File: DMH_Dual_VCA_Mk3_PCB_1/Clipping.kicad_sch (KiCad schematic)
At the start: 43 parts, among them SW1 SW_DPDT_OnOffOn_x2, U4 TL074, U8 TL074

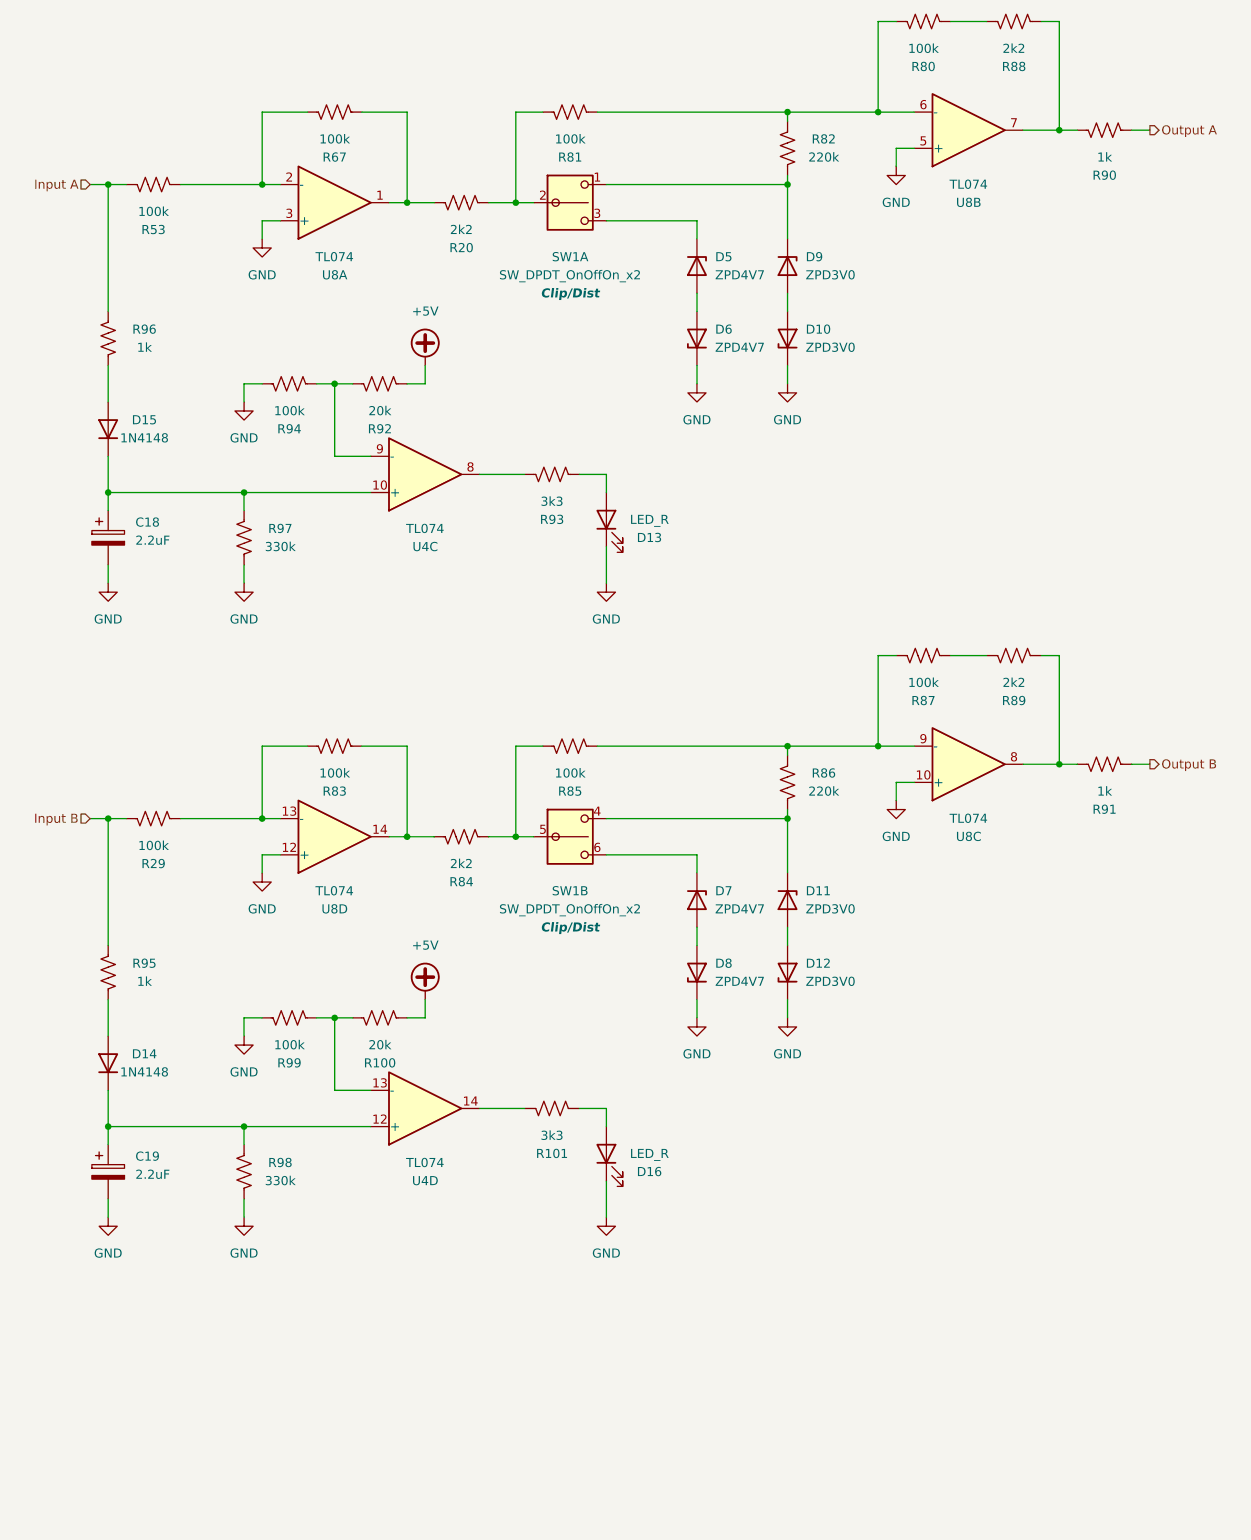
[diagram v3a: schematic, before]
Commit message: Improved cipping indication LED drive
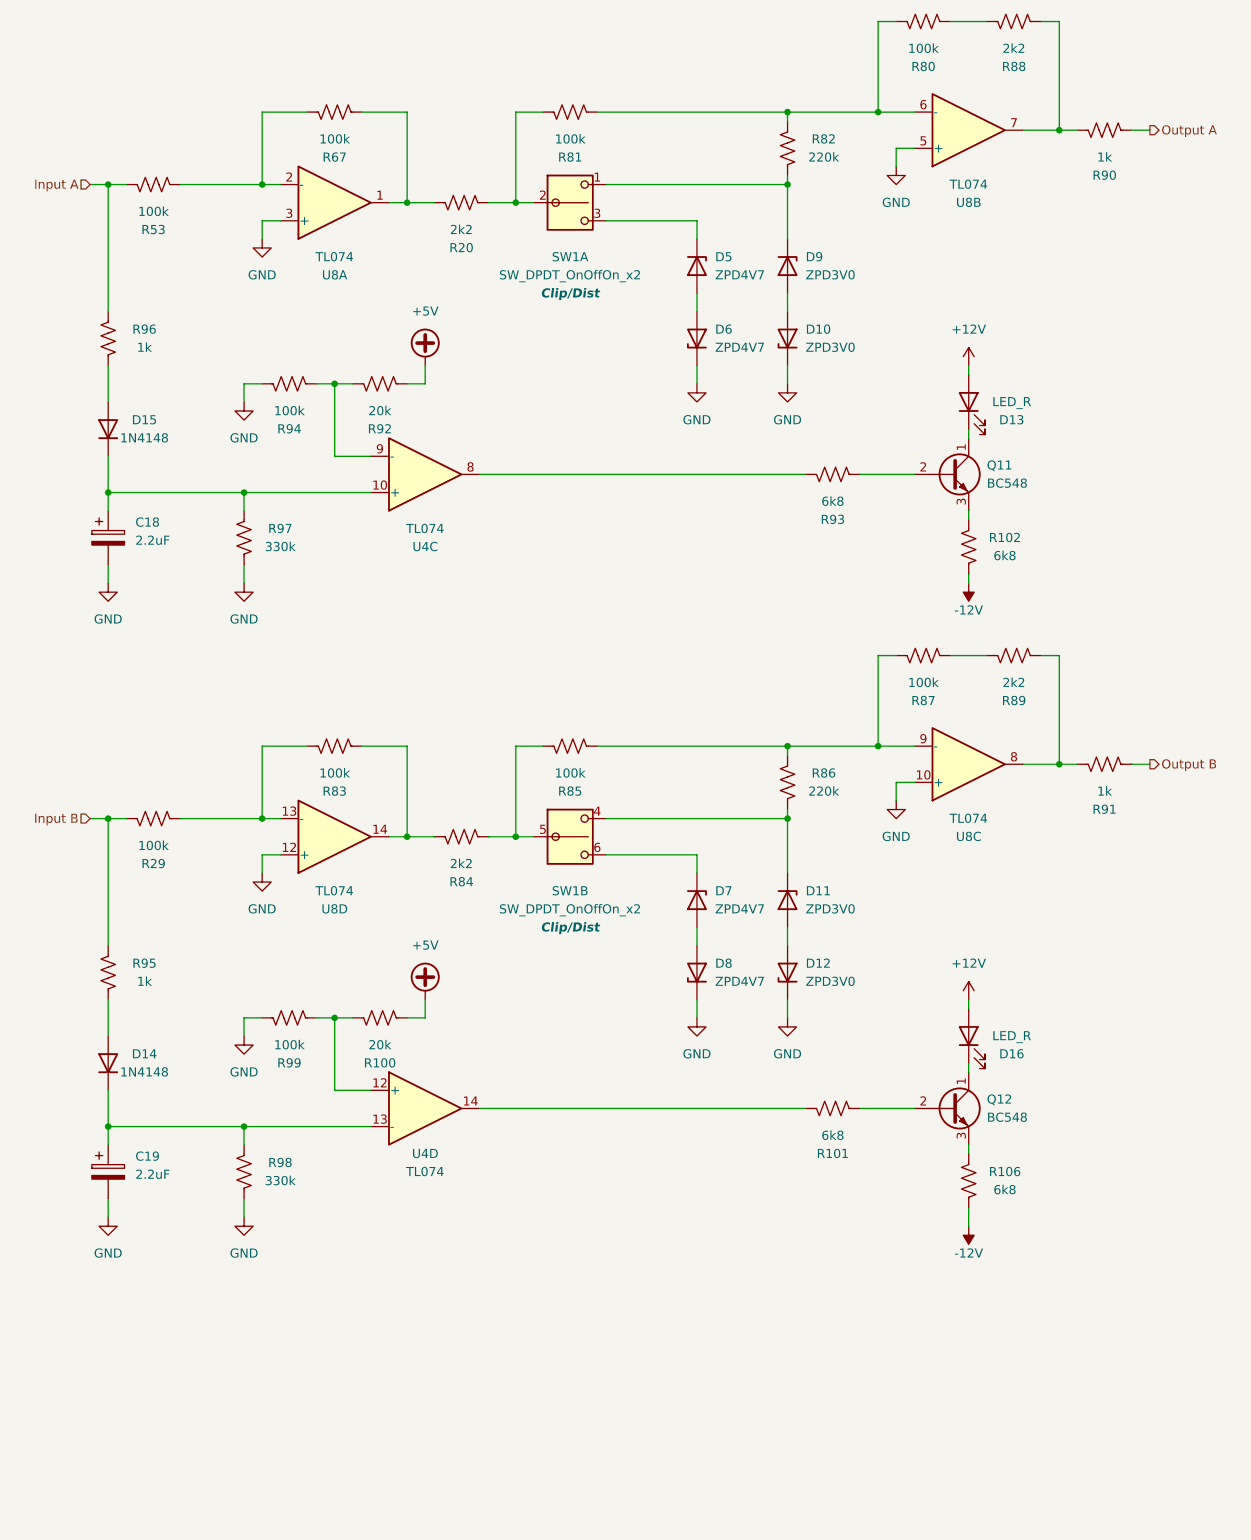
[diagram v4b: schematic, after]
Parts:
- added Q11: BC548, Package_TO_SOT_THT:TO-92_Inline, symbol Transistor_BJT:BC548
- added Q12: BC548, Package_TO_SOT_THT:TO-92L_Inline_Wide, symbol Transistor_BJT:BC548
- added R102, R106: 6k8, Resistor_THT:R_Axial_DIN0207_L6.3mm_D2.5mm_P7.62mm_Horizontal, symbol Device:R_US
- R101, R93: value 3k3 -> 6k8
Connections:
- net GND: no longer D13.1 (K), D16.1 (K)
- net at R93.2: now also Q11.2 (B); no longer D13.2 (A)
- net at R101.2: now also Q12.2 (B); no longer D16.2 (A)
- net at C19.1, D14.1 (K), R98.2: now also U4.13 (-); no longer U4.12 (+)
- net at R100.1, R99.2: now also U4.12 (+); no longer U4.13 (-)
- new net: D13.1 (K), Q11.1 (C)
- new net: Q11.3 (E), R102.2
- new net: D16.1 (K), Q12.1 (C)
- new net: Q12.3 (E), R106.2
- new net +12V: D13.2 (A), D16.2 (A)
- new net -12V: R102.1, R106.1
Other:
- moved on the sheet: D13, D16, R101, R93

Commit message: Improved clipping indicator
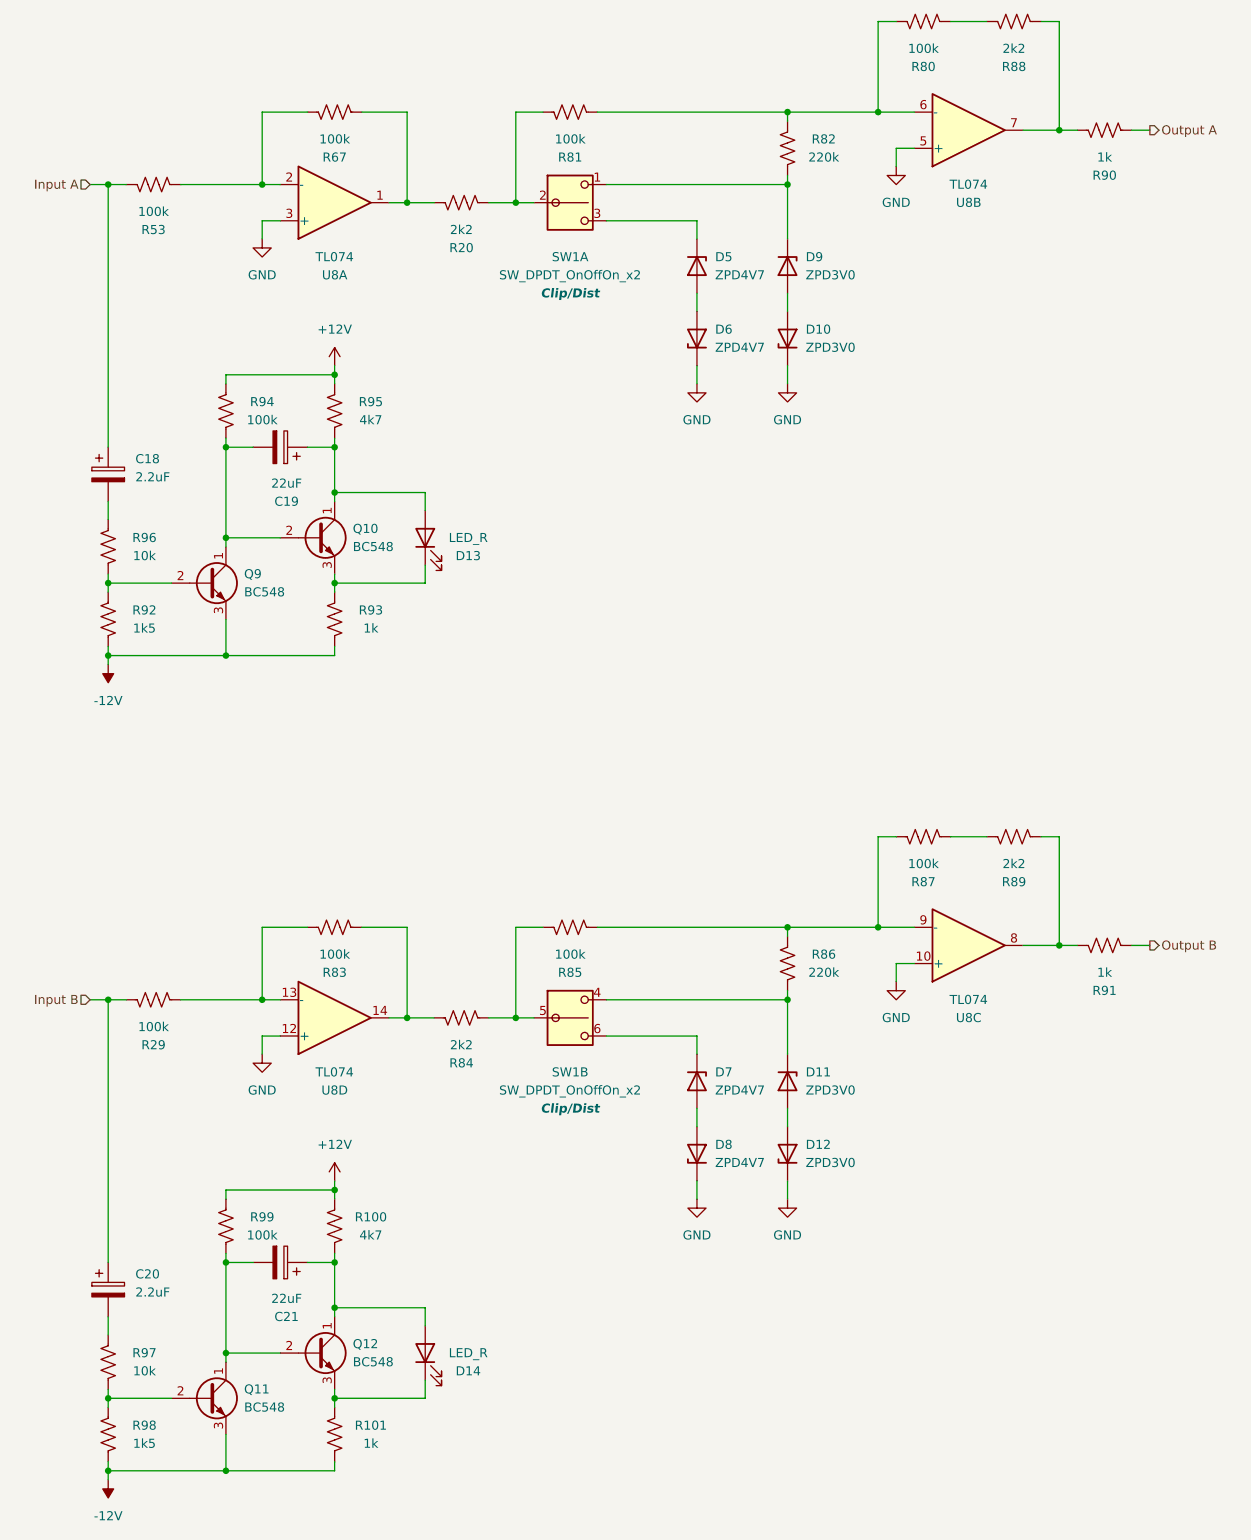
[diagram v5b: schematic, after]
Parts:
- removed D14, D15: 1N4148, Diode_THT:D_DO-35_SOD27_P7.62mm_Horizontal, symbol Diode:1N4148
- removed D16: LED_R, LED_THT:LED_D3.0mm, symbol Device:LED
- removed R102, R106: 6k8, Resistor_THT:R_Axial_DIN0207_L6.3mm_D2.5mm_P7.62mm_Horizontal, symbol Device:R_US
- removed U4: TL074, Package_DIP:DIP-14_W7.62mm_Socket, symbol Amplifier_Operational:TL074
- added C20: 2.2uF, Capacitor_THT:CP_Radial_D4.0mm_P1.50mm, symbol Device:C_Polarized
- added C21: 22uF, Capacitor_THT:CP_Radial_D4.0mm_P1.50mm, symbol Device:C_Polarized
- added D14: LED_R, LED_THT:LED_D3.0mm, symbol Device:LED
- added Q10, Q11: BC548, Package_TO_SOT_THT:TO-92_Inline, symbol Transistor_BJT:BC548
- C19: value 2.2uF -> 22uF
- Q12: footprint Package_TO_SOT_THT:TO-92L_Inline_Wide -> Package_TO_SOT_THT:TO-92_Inline
- R100: value 20k -> 4k7
- R101, R93: value 6k8 -> 1k
- R92: value 20k -> 1k5
- R95: value 1k -> 4k7
- R96: value 1k -> 10k
- R97: value 330k -> 10k
- R98: value 330k -> 1k5
- renumbered Q11 to Q9
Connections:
- net +12V: now also R100.2, R94.2, R95.2, R99.2; no longer D13.2 (A)
- net -12V: now also Q9.3 (E), R101.1, R92.1, R93.1, R98.1, Q11.3 (E)
- net GND: no longer C18.2, C19.2, R94.1, R97.1, R98.1, R99.1
- net Input A: now also C18.1; no longer R96.2
- net Input B: now also C20.1; no longer R95.2
- net at R96.1: now also Q9.2 (B), R92.2
- net at R97.2: now also C20.2; no longer C18.1
- net at Q9.1 (C): now also C19.2, R94.1, Q10.2 (B); no longer D13.1 (K)
- net at R93.2: now also D13.1 (K), Q10.3 (E); no longer Q9.2 (B)
- net at R95.1: now also C19.1, D13.2 (A), Q10.1 (C)
- net at Q12.1 (C): now also R100.1, C21.1, D14.2 (A)
- net at R98.2: now also R97.1, Q11.2 (B); no longer C19.1
- net at R101.2: now also Q12.3 (E), D14.1 (K); no longer Q12.2 (B)
- removed net +5V: R100.2, R92.2
- new net: C18.2, R96.2
- new net: C21.2, Q11.1 (C), Q12.2 (B), R99.1
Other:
- moved on the sheet: C18, D11, D12, D13, D7, D8, Q9, R29, R83, R84, R85, R86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
